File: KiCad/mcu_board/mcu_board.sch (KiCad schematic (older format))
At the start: 20 parts, among them IC1 ATMEGA328P-AU, IC2 74HC595D, P1 CONN_02X04, P2 ICSP, P3 CONN_01X06, P4 CONN_01X02, P5 CONN_01X03, P6 CONN_01X04, P7 CONN_01X10, U1 ESP-02, U2 ULN2803A, U3 ULN2803A, U4 TSOP38238

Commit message: Gerber
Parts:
- added C101: 4.7uF, Capacitors_ThroughHole:CP_Radial_D5.0mm_P2.50mm, symbol CP
- added R101: 150, Resistors_SMD:R_1206_HandSoldering, symbol R
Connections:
- net +3V3: now also R101.2
- net +5P: no longer U4.3
- net GND: now also C101.2
- new net: C101.1, R101.1, U4.3
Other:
- moved on the sheet: U4
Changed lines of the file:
@@
 L TSOP38238 U4
 U 1 1 58934C31
-P 9300 5100
-F 0 "U4" H 9250 5550 60  0000 C CNN
-F 1 "TSOP38238" H 9350 4600 60  0000 C CNN
-F 2 "franck:TSOP382" H 9300 5100 60  0001 C CNN
-F 3 "" H 9300 5100 60  0001 C CNN
-	1    9300 5100
+P 9300 5500
+F 0 "U4" H 9250 5950 60  0000 C CNN
+F 1 "TSOP38238" H 9350 5000 60  0000 C CNN
+F 2 "franck:TSOP382" H 9300 5500 60  0001 C CNN
+F 3 "" H 9300 5500 60  0001 C CNN
+	1    9300 5500
 	1    0    0    -1
 $EndComp
 $Comp
-L +5P #PWR028
-U 1 1 58934D12
-P 9800 4650
-F 0 "#PWR028" H 9800 4500 50  0001 C CNN
-F 1 "+5P" H 9800 4790 50  0000 C CNN
-F 2 "" H 9800 4650 50  0000 C CNN
-F 3 "" H 9800 4650 50  0000 C CNN
-	1    9800 4650
+L GND #PWR028
+U 1 1 58934E38
+P 9800 6000
+F 0 "#PWR028" H 9800 5750 50  0001 C CNN
+F 1 "GND" H 9800 5850 50  0000 C CNN
+F 2 "" H 9800 6000 50  0000 C CNN
+F 3 "" H 9800 6000 50  0000 C CNN
+	1    9800 6000
 	1    0    0    -1
 $EndComp
 Wire Wire Line
-	9800 4650 9800 4750
+	9700 5850 9800 5850
 Wire Wire Line
-	9800 4750 9700 4750
+	9800 5850 9800 6000
+Text Label 10300 5500 0    60   ~ 0
+IR-OUT
+Wire Wire Line
+	9700 5500 10300 5500
 $Comp
-L GND #PWR029
-U 1 1 58934E38
-P 9800 5550
-F 0 "#PWR029" H 9800 5300 50  0001 C CNN
-F 1 "GND" H 9800 5400 50  0000 C CNN
-F 2 "" H 9800 5550 50  0000 C CNN
-F 3 "" H 9800 5550 50  0000 C CNN
-	1    9800 5550
+L +3.3V #PWR029
+U 1 1 58983846
+P 10000 4750
+F 0 "#PWR029" H 10000 4600 50  0001 C CNN
+F 1 "+3.3V" H 10000 4890 50  0000 C CNN
+F 2 "" H 10000 4750 50  0000 C CNN
+F 3 "" H 10000 4750 50  0000 C CNN
+	1    10000 4750
+	1    0    0    -1
+$EndComp
+$Comp
+L R R101
+U 1 1 5898420B
+P 10000 4950
+F 0 "R101" V 10080 4950 50  0000 C CNN
+F 1 "150" V 10000 4950 50  0000 C CNN
+F 2 "Resistors_SMD:R_1206_HandSoldering" V 9930 4950 50  0001 C CNN
+F 3 "" H 10000 4950 50  0001 C CNN
+	1    10000 4950
+	-1   0    0    1
+$EndComp
+$Comp
+L CP C101
+U 1 1 58984258
+P 10000 5800
+F 0 "C101" H 10025 5900 50  0000 L CNN
+F 1 "4.7uF" H 10025 5700 50  0000 L CNN
+F 2 "Capacitors_ThroughHole:CP_Radial_D5.0mm_P2.50mm" H 10038 5650 50  0001 C CNN
+F 3 "" H 10000 5800 50  0001 C CNN
+	1    10000 5800
 	1    0    0    -1
 $EndComp
 Wire Wire Line
-	9700 5450 9800 5450
+	10000 5100 10000 5650
 Wire Wire Line
-	9800 5450 9800 5550
-Text Label 9800 5100 0    60   ~ 0
-IR-OUT
+	10000 5150 9700 5150
+Connection ~ 10000 5150
 Wire Wire Line
-	9700 5100 9800 5100
+	10000 4750 10000 4800
+$Comp
+L GND #PWR030
+U 1 1 58987B9C
+P 10000 6000
+F 0 "#PWR030" H 10000 5750 50  0001 C CNN
+F 1 "GND" H 10000 5850 50  0000 C CNN
+F 2 "" H 10000 6000 50  0000 C CNN
+F 3 "" H 10000 6000 50  0000 C CNN
+	1    10000 6000
+	1    0    0    -1
+$EndComp
+Wire Wire Line
+	10000 5950 10000 6000
 $EndSCHEMATC

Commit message: Correctifs divers
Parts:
- U1: footprint franck:ESP_02_SMD_Handsoldering -> flem:ESP8266_ESP_02_SMD_Handsoldering
- U4: footprint franck:TSOP382 -> flem:TSOP382
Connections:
- net ESP-RX: now also P1.5 (P5); no longer P1.3 (P3)
- net ESP-TX: now also P1.3 (P3); no longer P1.5 (P5)
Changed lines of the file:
@@
 F 0 "U1" H 3150 950 50  0000 C CNN
 F 1 "ESP-02" H 3150 1150 50  0000 C CNN
-F 2 "franck:ESP_02_SMD_Handsoldering" H 3150 1050 50  0001 C CNN
+F 2 "flem:ESP8266_ESP_02_SMD_Handsoldering" H 3150 1050 50  0001 C CNN
 F 3 "" H 3150 1050 50  0001 C CNN
 	1    3150 1050
@@
 	1    0    0    -1
 $EndComp
+Text Label 1200 2350 2    60   ~ 0
+ESP-RX
 Text Label 1200 2250 2    60   ~ 0
-ESP-RX
-Text Label 1200 2350 2    60   ~ 0
 ESP-TX
 Text Label 2000 900  2    60   ~ 0
@@
 F 0 "U4" H 9250 5950 60  0000 C CNN
 F 1 "TSOP38238" H 9350 5000 60  0000 C CNN
-F 2 "franck:TSOP382" H 9300 5500 60  0001 C CNN
+F 2 "flem:TSOP382" H 9300 5500 60  0001 C CNN
 F 3 "" H 9300 5500 60  0001 C CNN
 	1    9300 5500

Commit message: Gerber
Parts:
- added P106: CONN_01X02, Pin_Headers:Pin_Header_Straight_1x02_Pitch2.54mm, symbol CONN_01X02
- renumbered C3 to C101, C4 to C102, C1 to C103, C101 to C104, IC1 to IC101, IC2 to IC102, JP1 to JP101, JP2 to JP102, P1 to P101, P2 to P102, P3 to P103, P4 to P104, P5 to P105, P6 to P107, P7 to P108, R1 to R101, R2 to R102, R101 to R103, U1 to U101, U2 to U102, U3 to U103, U4 to U104
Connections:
- net ESP-GPIO2: no longer JP102.1
- net ESP-RST: now also JP102.1
- net FU2: now reaches IC101.10 ((PCINT22/OC0A/AIN0)PD6)
- net FU2: now also U103.5 (I5)
- net FU1: now reaches IC101.9 ((PCINT21/OC0B/T1)PD5)
- net FU1: now also U103.4 (I4)
- net K-FU2: now reaches U103.14 (O5)
- net K-FU2: now also P106.2 (P2)
- net K-FU1: now reaches U103.15 (O4)
- net K-FU1: now also P106.1 (P1)
- net ESP-GPIO15 renamed ESP-CHPD
- no-connect marks 24 -> 18
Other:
- moved on the sheet: JP102
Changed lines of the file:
@@
 $EndDescr
 $Comp
-L ATMEGA328P-AU IC1
+L ATMEGA328P-AU IC101
 U 1 1 5882126A
 P 4750 3300
-F 0 "IC1" H 4000 4550 50  0000 L BNN
+F 0 "IC101" H 4000 4550 50  0000 L BNN
 F 1 "ATMEGA328P-AU" H 5150 1900 50  0000 L BNN
 F 2 "Housings_QFP:TQFP-32_7x7mm_Pitch0.8mm" H 4750 3300 50  0001 C CIN
@@
 $EndComp
 $Comp
-L CONN_02X03 P2
+L CONN_02X03 P102
 U 1 1 588281DD
 P 1500 3350
-F 0 "P2" H 1500 3550 50  0000 C CNN
+F 0 "P102" H 1500 3550 50  0000 C CNN
 F 1 "ICSP" H 1500 3150 50  0000 C CNN
 F 2 "Pin_Headers:Pin_Header_Straight_2x03_Pitch2.54mm" H 1500 2150 50  0001 C CNN
@@
 RCLK
 $Comp
-L CONN_01X10 P7
+L CONN_01X10 P108
 U 1 1 5883769A
 P 10300 1450
-F 0 "P7" H 10300 2000 50  0000 C CNN
+F 0 "P108" H 10300 2000 50  0000 C CNN
 F 1 "CONN_01X10" V 10400 1450 50  0000 C CNN
 F 2 "Pin_Headers:Pin_Header_Straight_1x10_Pitch2.54mm" H 10300 1450 50  0001 C CNN
@@
 $EndComp
 $Comp
-L R R1
+L R R101
 U 1 1 5883B3E9
 P 6050 6700
-F 0 "R1" V 6130 6700 50  0000 C CNN
+F 0 "R101" V 6130 6700 50  0000 C CNN
 F 1 "10K" V 6050 6700 50  0000 C CNN
 F 2 "Resistors_SMD:R_1206_HandSoldering" V 5980 6700 50  0001 C CNN
@@
 SCL
 $Comp
-L R R2
+L R R102
 U 1 1 5883C946
 P 6050 6900
-F 0 "R2" V 6130 6900 50  0000 C CNN
+F 0 "R102" V 6130 6900 50  0000 C CNN
 F 1 "10K" V 6050 6900 50  0000 C CNN
 F 2 "Resistors_SMD:R_1206_HandSoldering" V 5980 6900 50  0001 C CNN
@@
 NoConn ~ 9700 1900
 $Comp
-L ESP-02 U1
+L ESP-02 U101
 U 1 1 58826750
 P 3150 1050
-F 0 "U1" H 3150 950 50  0000 C CNN
+F 0 "U101" H 3150 950 50  0000 C CNN
 F 1 "ESP-02" H 3150 1150 50  0000 C CNN
 F 2 "flem:ESP8266_ESP_02_SMD_Handsoldering" H 3150 1050 50  0001 C CNN
@@
 ESP-RX
 $Comp
-L C C1
+L C C103
 U 1 1 5882B9E5
 P 7700 3350
-F 0 "C1" H 7725 3450 50  0000 L CNN
+F 0 "C103" H 7725 3450 50  0000 L CNN
 F 1 "100nF" H 7725 3250 50  0000 L CNN
 F 2 "Capacitors_SMD:C_0603_HandSoldering" H 7738 3200 50  0001 C CNN
@@
 ESP-GPIO0
 Text Label 4150 1200 0    60   ~ 0
-ESP-GPIO15
+ESP-CHPD
 Text Label 1800 2150 0    60   ~ 0
 ESP-RST
@@
 ESP-GPIO0
 Text Label 1800 2450 0    60   ~ 0
-ESP-GPIO15
-$Comp
-L ULN2803A U2
+ESP-CHPD
+$Comp
+L ULN2803A U102
 U 1 1 588506FE
 P 9300 1400
-F 0 "U2" H 9300 1925 50  0000 C CNN
+F 0 "U102" H 9300 1925 50  0000 C CNN
 F 1 "ULN2803A" H 9300 1850 50  0000 C CNN
 F 2 "Housings_SOIC:SOIC-18W_7.5x11.6mm_Pitch1.27mm" H 9350 750 50  0001 L CNN
@@
 $EndComp
 $Comp
-L 74HC595D IC2
+L 74HC595D IC102
 U 1 1 588570EE
 P 7700 1500
-F 0 "IC2" H 7400 2025 50  0000 L BNN
+F 0 "IC102" H 7400 2025 50  0000 L BNN
 F 1 "74HC595D" H 7400 800 50  0000 L BNN
 F 2 "SMD_Packages:SO-16-N" H 7700 1650 50  0001 C CNN
@@
 $EndComp
 $Comp
-L 74HC595D IC2
+L 74HC595D IC102
 U 2 1 588571ED
 P 7400 3350
-F 0 "IC2" H 7250 3750 50  0000 L BNN
+F 0 "IC102" H 7250 3750 50  0000 L BNN
 F 1 "74HC595D" V 7300 3100 50  0000 L BNN
 F 2 "SMD_Packages:SO-16-N" H 7400 3500 50  0001 C CNN
@@
 Text Label 5950 4000 0    60   ~ 0
 PWR_PRE
-NoConn ~ 5750 4300
-NoConn ~ 5750 4400
 NoConn ~ 5750 4500
 $Comp
-L ULN2803A U3
+L ULN2803A U103
 U 1 1 5887E88A
 P 9300 3200
-F 0 "U3" H 9300 3725 50  0000 C CNN
+F 0 "U103" H 9300 3725 50  0000 C CNN
 F 1 "ULN2803A" H 9300 3650 50  0000 C CNN
 F 2 "Housings_SOIC:SOIC-18W_7.5x11.6mm_Pitch1.27mm" H 9350 2550 50  0001 L CNN
@@
 	1    0    0    -1
 $EndComp
-NoConn ~ 9700 3200
-NoConn ~ 9700 3300
 NoConn ~ 9700 3400
 NoConn ~ 9700 3500
 NoConn ~ 9700 3600
 NoConn ~ 9700 3700
-NoConn ~ 8900 3200
-NoConn ~ 8900 3300
 NoConn ~ 8900 3400
 NoConn ~ 8900 3500
@@
 K-AlimAmpli
 $Comp
-L CONN_01X02 P4
+L CONN_01X02 P104
 U 1 1 58894554
 P 2650 7050
-F 0 "P4" H 2600 7200 50  0000 C CNN
+F 0 "P104" H 2600 7200 50  0000 C CNN
 F 1 "CONN_01X02" V 2750 7050 50  0000 C CNN
 F 2 "Pin_Headers:Pin_Header_Straight_1x02_Pitch2.54mm" H 2650 7050 50  0001 C CNN
@@
 NoConn ~ 5750 2300
 $Comp
-L CONN_01X03 P5
+L CONN_01X03 P105
 U 1 1 5888E7CB
 P 4350 5800
-F 0 "P5" H 4300 6000 50  0000 C CNN
+F 0 "P105" H 4300 6000 50  0000 C CNN
 F 1 "CONN_01X03" V 4450 5800 50  0000 C CNN
 F 2 "Pin_Headers:Pin_Header_Straight_1x03_Pitch2.54mm" H 4350 5800 50  0001 C CNN
@@
 Text Label 5950 2400 0    60   ~ 0
 LED_DIN
-Text Label 5800 1000 0    60   ~ 0
+Text Label 5800 900  0    60   ~ 0
 RESET
 $Comp
-L Jumper JP2
+L Jumper JP102
 U 1 1 588A850B
-P 5200 1000
-F 0 "JP2" H 5200 1150 60  0000 C CNN
-F 1 "JUMPER" H 5200 920 40  0000 C CNN
-F 2 "Measurement_Points:Test_Point_2Pads" H 5200 1000 60  0001 C CNN
-F 3 "" H 5200 1000 60  0000 C CNN
-	1    5200 1000
-	1    0    0    -1
-$EndComp
-$Comp
-L Jumper JP1
+P 5200 900
+F 0 "JP102" H 5200 1050 60  0000 C CNN
+F 1 "JUMPER" H 5200 820 40  0000 C CNN
+F 2 "Measurement_Points:Test_Point_2Pads" H 5200 900 60  0001 C CNN
+F 3 "" H 5200 900 60  0000 C CNN
+	1    5200 900
+	1    0    0    -1
+$EndComp
+$Comp
+L Jumper JP101
 U 1 1 588A897F
 P 1150 1200
-F 0 "JP1" H 1150 1350 60  0000 C CNN
+F 0 "JP101" H 1150 1350 60  0000 C CNN
 F 1 "JUMPER" H 1150 1120 40  0000 C CNN
 F 2 "Measurement_Points:Test_Point_2Pads" H 1150 1200 60  0001 C CNN
@@
 $EndComp
 $Comp
-L CONN_02X04 P1
+L CONN_02X04 P101
 U 1 1 588F5911
 P 1500 2300
-F 0 "P1" H 1500 2550 50  0000 C CNN
+F 0 "P101" H 1500 2550 50  0000 C CNN
 F 1 "CONN_02X04" H 1500 2050 50  0000 C CNN
 F 2 "Pin_Headers:Pin_Header_Straight_2x04_Pitch2.54mm" H 1500 1100 50  0001 C CNN
@@
 $EndComp
 $Comp
-L CONN_01X04 P6
+L CONN_01X04 P107
 U 1 1 58914CD3
 P 6050 5850
-F 0 "P6" H 6050 6100 50  0000 C CNN
+F 0 "P107" H 6050 6100 50  0000 C CNN
 F 1 "CONN_01X04" V 6150 5850 50  0000 C CNN
 F 2 "Pin_Headers:Pin_Header_Straight_1x04_Pitch2.54mm" H 6050 5850 50  0001 C CNN
@@
 K-AlimPreamp
 $Comp
-L CONN_01X06 P3
+L CONN_01X06 P103
 U 1 1 5890E244
 P 2650 5950
-F 0 "P3" H 2650 6300 50  0000 C CNN
+F 0 "P103" H 2650 6300 50  0000 C CNN
 F 1 "CONN_01X06" V 2750 5950 50  0000 C CNN
 F 2 "Pin_Headers:Pin_Header_Straight_1x06_Pitch2.54mm" H 2650 5950 50  0001 C CNN
@@
 $EndComp
 $Comp
-L C C3
+L C C101
 U 1 1 58920900
 P 3100 2300
-F 0 "C3" H 3125 2400 50  0000 L CNN
+F 0 "C101" H 3125 2400 50  0000 L CNN
 F 1 "100nF" H 3125 2200 50  0000 L CNN
 F 2 "Capacitors_SMD:C_0603_HandSoldering" H 3138 2150 50  0001 C CNN
@@
 $EndComp
 $Comp
-L CP C4
+L CP C102
 U 1 1 58920B5C
 P 3400 2300
-F 0 "C4" H 3425 2400 50  0000 L CNN
+F 0 "C102" H 3425 2400 50  0000 L CNN
 F 1 "10uF" H 3425 2200 50  0000 L CNN
 F 2 "Capacitors_ThroughHole:CP_Radial_D5.0mm_P2.50mm" H 3438 2150 50  0001 C CNN
@@
 Connection ~ 7550 3700
 Wire Wire Line
-	4100 900  4150 900
-Wire Wire Line
-	4100 1000 4900 1000
+	4100 900  4900 900
 Wire Wire Line
 	4100 1100 4150 1100
@@
 	5750 2200 5950 2200
 Wire Wire Line
-	5500 1000 5800 1000
+	5500 900  5800 900
 Connection ~ 2150 900
 Wire Wire Line
@@
 NoConn ~ 5750 4200
 $Comp
-L TSOP38238 U4
+L TSOP38238 U104
 U 1 1 58934C31
 P 9300 5500
-F 0 "U4" H 9250 5950 60  0000 C CNN
+F 0 "U104" H 9250 5950 60  0000 C CNN
 F 1 "TSOP38238" H 9350 5000 60  0000 C CNN
 F 2 "flem:TSOP382" H 9300 5500 60  0001 C CNN
@@
 $EndComp
 $Comp
-L R R101
+L R R103
 U 1 1 5898420B
 P 10000 4950
-F 0 "R101" V 10080 4950 50  0000 C CNN
+F 0 "R103" V 10080 4950 50  0000 C CNN
 F 1 "150" V 10000 4950 50  0000 C CNN
 F 2 "Resistors_SMD:R_1206_HandSoldering" V 9930 4950 50  0001 C CNN
@@
 $EndComp
 $Comp
-L CP C101
+L CP C104
 U 1 1 58984258
 P 10000 5800
-F 0 "C101" H 10025 5900 50  0000 L CNN
+F 0 "C104" H 10025 5900 50  0000 L CNN
 F 1 "4.7uF" H 10025 5700 50  0000 L CNN
 F 2 "Capacitors_ThroughHole:CP_Radial_D5.0mm_P2.50mm" H 10038 5650 50  0001 C CNN
@@
 Wire Wire Line
 	10000 5950 10000 6000
+Text Label 5950 4300 0    60   ~ 0
+FU1
+Text Label 5950 4400 0    60   ~ 0
+FU2
+Wire Wire Line
+	5950 4300 5750 4300
+Wire Wire Line
+	5950 4400 5750 4400
+Text Label 8650 3200 2    60   ~ 0
+FU1
+Text Label 8650 3300 2    60   ~ 0
+FU2
+Wire Wire Line
+	8650 3200 8900 3200
+Wire Wire Line
+	8650 3300 8900 3300
+Text Label 9950 3200 0    60   ~ 0
+K-FU1
+Text Label 9950 3300 0    60   ~ 0
+K-FU2
+Wire Wire Line
+	9700 3200 9950 3200
+Wire Wire Line
+	9700 3300 9950 3300
+$Comp
+L CONN_01X02 P106
+U 1 1 589BCB71
+P 4350 7050
+F 0 "P106" H 4300 7200 50  0000 C CNN
+F 1 "CONN_01X02" V 4450 7050 50  0000 C CNN
+F 2 "Pin_Headers:Pin_Header_Straight_1x02_Pitch2.54mm" H 4350 7050 50  0001 C CNN
+F 3 "" H 4350 7050 50  0000 C CNN
+	1    4350 7050
+	1    0    0    -1
+$EndComp
+Text Label 4050 7000 2    60   ~ 0
+K-FU1
+Text Label 4050 7100 2    60   ~ 0
+K-FU2
+Wire Wire Line
+	4050 7000 4150 7000
+Wire Wire Line
+	4050 7100 4150 7100
+Wire Wire Line
+	4100 1000 4150 1000
 $EndSCHEMATC

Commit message: Divers
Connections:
- net ESP-GPIO2: now also JP102.1
- net ESP-RST: no longer JP102.1
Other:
- note added: "Futur use with OTA programming"
- moved on the sheet: JP102
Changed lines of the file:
@@
 Text Label 5950 2400 0    60   ~ 0
 LED_DIN
-Text Label 5800 900  0    60   ~ 0
+Text Label 5800 1000 0    60   ~ 0
 RESET
 $Comp
 L Jumper JP102
 U 1 1 588A850B
-P 5200 900
-F 0 "JP102" H 5200 1050 60  0000 C CNN
-F 1 "JUMPER" H 5200 820 40  0000 C CNN
-F 2 "Measurement_Points:Test_Point_2Pads" H 5200 900 60  0001 C CNN
-F 3 "" H 5200 900 60  0000 C CNN
-	1    5200 900
+P 5200 1000
+F 0 "JP102" H 5200 1150 60  0000 C CNN
+F 1 "JUMPER" H 5200 920 40  0000 C CNN
+F 2 "Measurement_Points:Test_Point_2Pads" H 5200 1000 60  0001 C CNN
+F 3 "" H 5200 1000 60  0000 C CNN
+	1    5200 1000
 	1    0    0    -1
 $EndComp
@@
 Connection ~ 7550 3700
 Wire Wire Line
-	4100 900  4900 900
-Wire Wire Line
 	4100 1100 4150 1100
 Wire Wire Line
@@
 	5750 2200 5950 2200
 Wire Wire Line
-	5500 900  5800 900
+	5500 1000 5800 1000
 Connection ~ 2150 900
 Wire Wire Line
@@
 	4050 7100 4150 7100
 Wire Wire Line
-	4100 1000 4150 1000
+	4100 1000 4900 1000
+Wire Wire Line
+	4100 900  4150 900
+Text Notes 4850 800  0    60   ~ 0
+Futur use with OTA programming
 $EndSCHEMATC

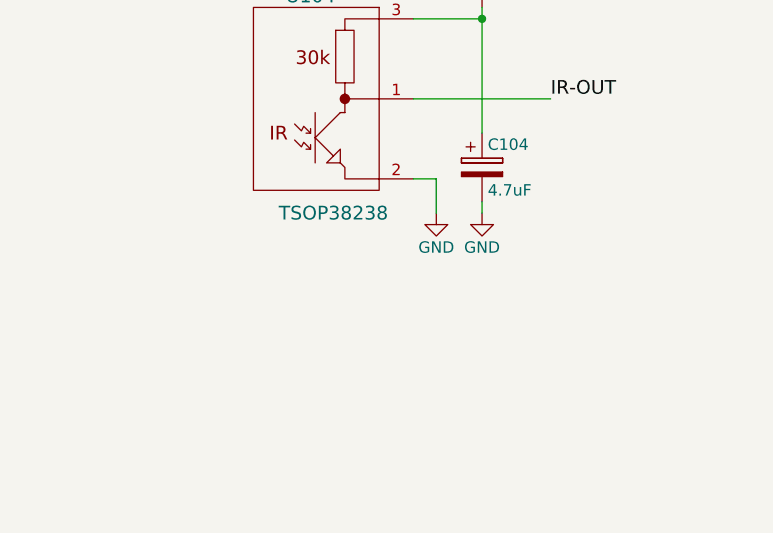
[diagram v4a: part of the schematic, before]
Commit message: PCB mcu_board: RC5 + REC-80 (panasonic) IR protocols
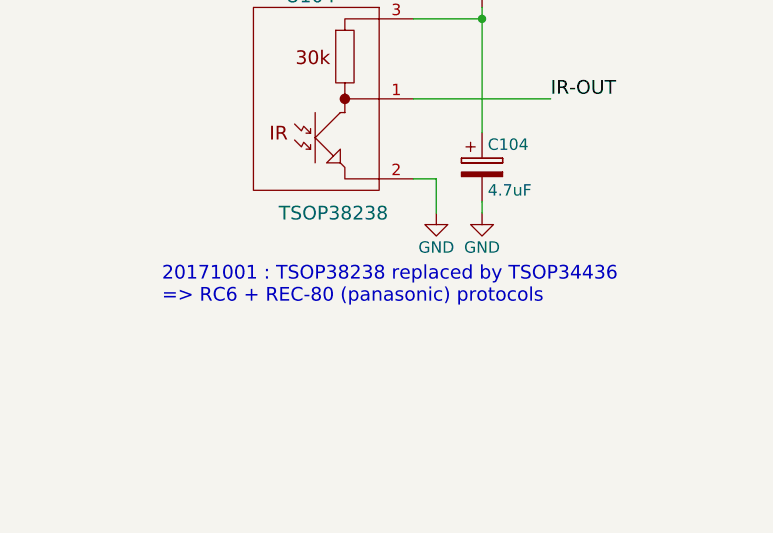
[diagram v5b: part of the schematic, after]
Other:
- note added: "20171001 : TSOP38238 replaced by TSOP34436\n=> RC6 + REC-80 (panasonic) protocols"
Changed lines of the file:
@@
 Text Notes 4850 800  0    60   ~ 0
 Futur use with OTA programming
+Text Notes 8600 6400 0    60   ~ 0
+20171001 : TSOP38238 replaced by TSOP34436\n=> RC6 + REC-80 (panasonic) protocols
 $EndSCHEMATC

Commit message: Divers
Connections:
- net hp renamed s8
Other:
- note added: "FU1"
- note added: "FU2"
- note added: "S6 (By-Pass)"
- note removed: "HP-Phone"
- note removed: "S6"
- note removed: "S7"
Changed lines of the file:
@@
 	3400 2450 3400 2500
 Text Label 8250 1800 0    60   ~ 0
-hp
+s8
 Wire Wire Line
 	8200 1800 8250 1800
@@
 	8200 1100 8250 1100
 Text Label 8850 1200 2    60   ~ 0
-hp
+s8
 Text Label 8850 1300 2    60   ~ 0
 s7
@@
 S5
 Text Notes 10500 1400 0    60   Italic 0
-S6
+S6 (By-Pass)
 Text Notes 10500 1300 0    60   Italic 0
-S7
+FU1
 Text Notes 10500 1200 0    60   Italic 0
-HP-Phone
+FU2
 Wire Wire Line
 	5750 2400 5950 2400
